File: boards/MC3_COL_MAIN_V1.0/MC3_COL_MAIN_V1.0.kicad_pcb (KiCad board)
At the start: 4 copper layers, 66 x 66 mm, 109 parts, among them J1 SUPPLY_IN, J10 MOTOR, J11 MOTOR, J12 CAN, J2 SWD, J3 ENC_leaf1, J4 ENC_leaf2, J5 ENC_leaf3, J6 ENC_leaf4, J7 MOTOR, J8 MOTOR, J9 MOTOR, Q1 AO4407C, SW1 SKRKAEE020, U1 AMS1117-3.3, U2 STM32F412RET6, U3 DRV8214RTER, U4 DRV8214RTER, U5 DRV8214RTER, U6 DRV8214RTER, U7 DRV8214RTER, U8 TJA1051T/3, Y1 8MHz

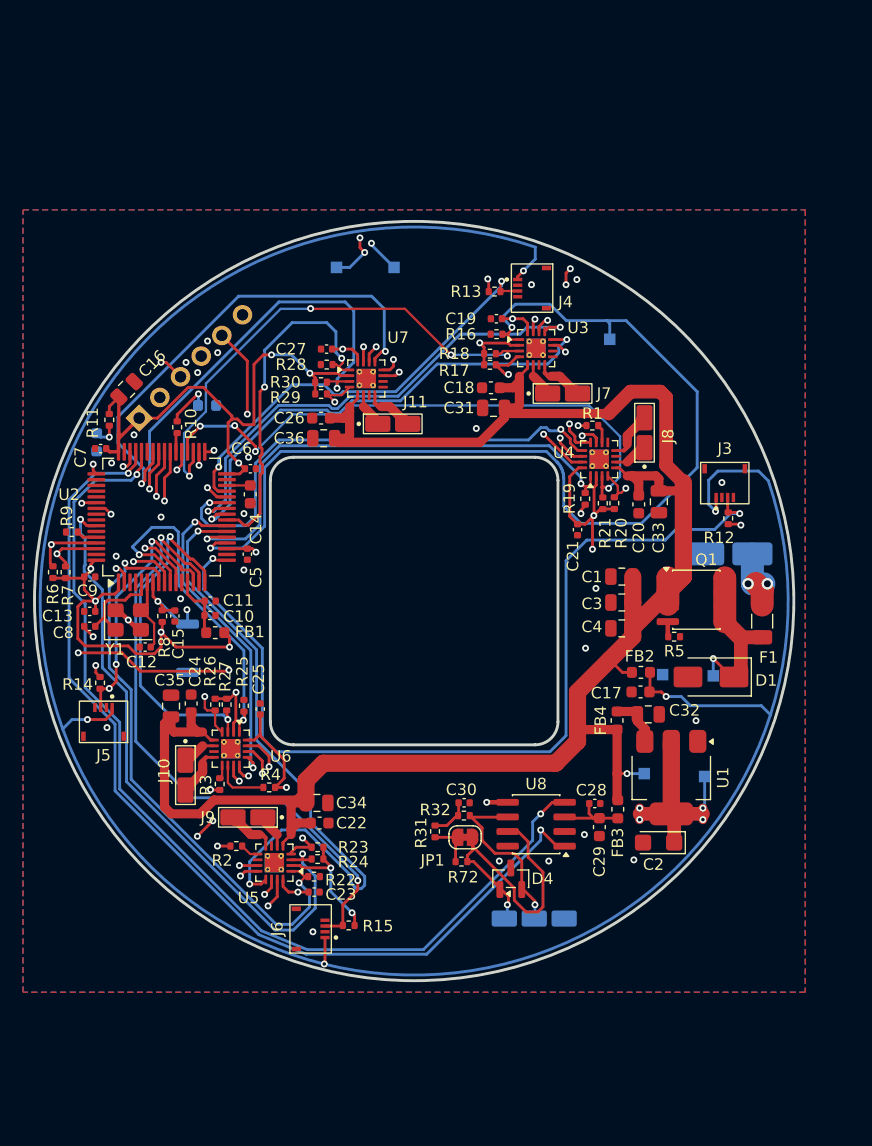
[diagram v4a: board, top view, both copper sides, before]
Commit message: Review fixes applied (C21, C37 order, stitching vias) + review-driven adds: 5x 1nF IPROPI ADC filters (C38-42, C1523), U8 VIO 100nF (C43), 3x M2.5 NPTH mounting holes (H1-3) - caps placed unwired, user wires; holes placed in layout by user
Co-Authored-By: Claude Fable 5 <noreply@anthropic.com>
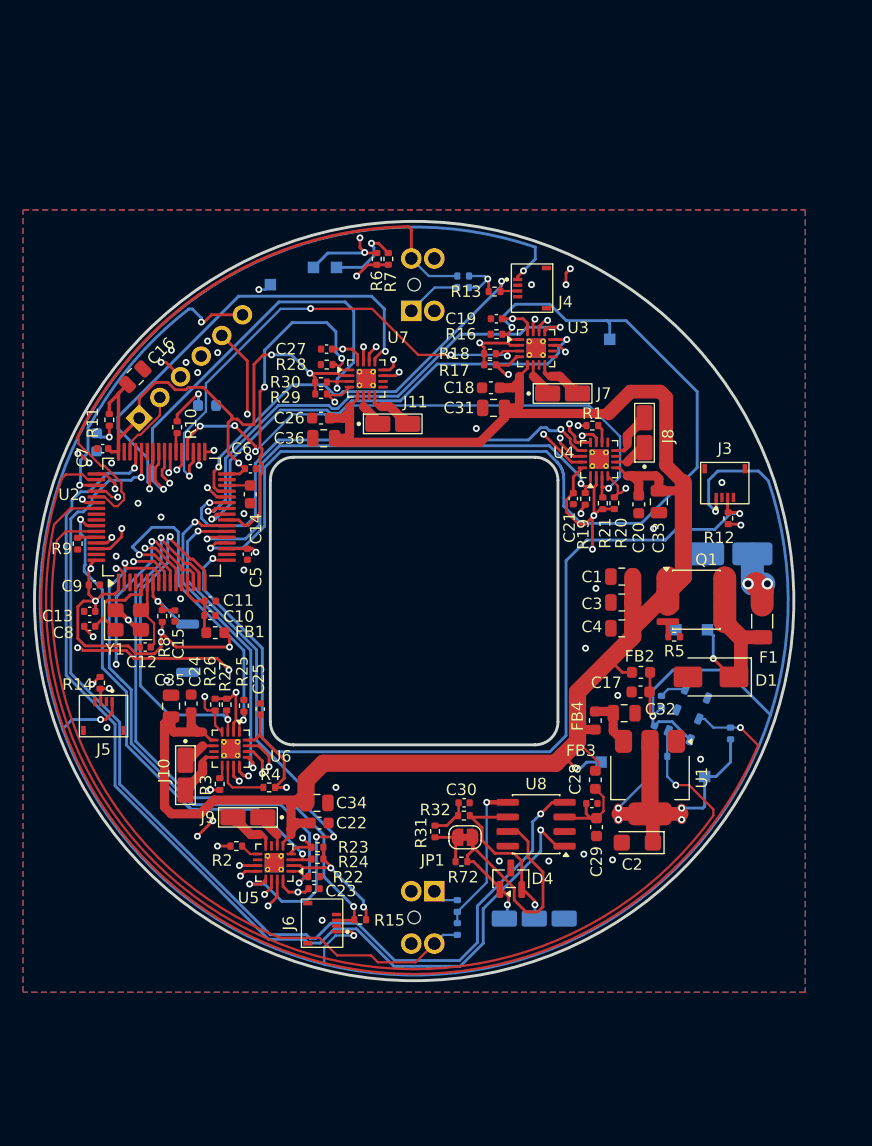
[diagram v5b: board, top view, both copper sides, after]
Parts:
- added C37: 100nF, MC3_COL_MAIN:C_0402_1005Metric, B.Cu at (120.7, 111.3)
- added R33: 220R, MC3_COL_MAIN:R_0402_1005Metric, B.Cu at (121.5, 108.8)
- added R34: 2.2k, MC3_COL_MAIN:R_0402_1005Metric, B.Cu at (127.5, 111.5)
- added R35: 2.2k, MC3_COL_MAIN:R_0402_1005Metric, B.Cu at (121.5, 113.5)
- added R36: 100R, MC3_COL_MAIN:R_0402_1005Metric, B.Cu at (103.8, 126.5)
- added R37: 47k, MC3_COL_MAIN:R_0402_1005Metric, B.Cu at (103.8, 128.5)
- added R38: 100R, MC3_COL_MAIN:R_0402_1005Metric, B.Cu at (104.3, 72.8)
- added R39: 47k, MC3_COL_MAIN:R_0402_1005Metric, B.Cu at (104.3, 71.8)
- added TP8: DBG_RX, MC3_COL_MAIN:TestPoint_Pad_1.0x1.0mm, B.Cu at (87.5, 72.5)
- added U10: GP1S094HCZ0F, MC3_COL_MAIN:GP1S094HCZ0F, B.Cu at (100.8, 127.5)
- added U11: GP1S094HCZ0F, MC3_COL_MAIN:GP1S094HCZ0F, B.Cu at (100.8, 72.5)
- added U9: AEDR-8300-1Q0, MC3_COL_MAIN:AEDR-8300, B.Cu at (123.8, 109.9)
- moved R6 39.2 mm to (96.8, 70.3)
- moved R7 39.1 mm to (97.8, 70.3)
- moved TP5 5.00 mm to (93.2, 71.0)
- moved TP7 4.07 mm to (122.8, 102.5)
- moved TP2 4.03 mm to (125.5, 102.5)
- moved TP1 3.88 mm to (116.2, 114.0)
- moved FB3 3.22 mm to (115.8, 115.5)
- moved C21 2.73 mm to (113.8, 91.1)
- moved C32 2.10 mm to (118.2, 109.8)
- moved TP4 2.00 mm to (91.2, 71.0)
- moved FB4 1.89 mm to (115.8, 110.4)
- moved C2 1.85 mm to (119.4, 121.0)
- moved U1 1.85 mm to (120.5, 115.3)
- moved C16 1.33 mm to (75.8, 80.5)
- moved R9 1.13 mm to (70.8, 95.0), turned to -90 degrees
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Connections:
- net /Connectors/VSENS renamed VSENS
- J2 pad 6: /MCU/SWO -> /MCU/DBG_TX
- U2 pad 50: unconnected-(U2-PA15-Pad50) -> /MCU/YAW_ENC_A
- U2 pad 51: unconnected-(U2-PC10-Pad51) -> /MCU/DBG_TX
- U2 pad 52: unconnected-(U2-PC11-Pad52) -> /MCU/DBG_RX
- U2 pad 53: unconnected-(U2-PC12-Pad53) -> /MCU/YAW_LIM
- U2 pad 55: /MCU/SWO -> /MCU/YAW_ENC_B
- U2 pad 59: unconnected-(U2-PB7-Pad59) -> /MCU/YAW_HOME
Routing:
- net +3V3: track 194.9 -> 225.5 mm, vias 29 -> 30
- net /MCU/DBG_RX: track 0.00 -> 26.9 mm, vias 0 -> 2
- net /MCU/SWO: track 25.0 -> 0.00 mm, vias 1 -> 0
- net /MCU/YAW_HOME: track 0.00 -> 21.0 mm
- net /MCU/YAW_LIM: track 0.00 -> 17.6 mm
- net VSENS: track 34.4 -> 50.4 mm
- net /MCU/YAW_ENC_B: track 0.00 -> 14.0 mm, vias 0 -> 1
- net /MCU/DBG_TX: track 0.00 -> 12.8 mm, vias 0 -> 2
- net I2C1_SDA: track 82.7 -> 94.6 mm, vias 8 -> 7
- net RC_OUT_leaf3: track 56.2 -> 44.5 mm
- net /MCU/YAW_ENC_A: track 0.00 -> 9.44 mm, vias 0 -> 1
- net EN_leaf3: track 57.3 -> 49.3 mm, vias 2 -> 4
- net I2C1_SCL: track 89.2 -> 96.5 mm, vias 10 -> 12
- net nFAULT_yaw: track 29.1 -> 24.2 mm
- net Net-(U11-A): track 0.00 -> 4.84 mm
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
